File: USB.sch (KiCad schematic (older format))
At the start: 25 parts, among them J1 USB_C_Receptacle, U1 IMX8MM, U2 NX20P3483UK, U6 PTN5110NHQZ

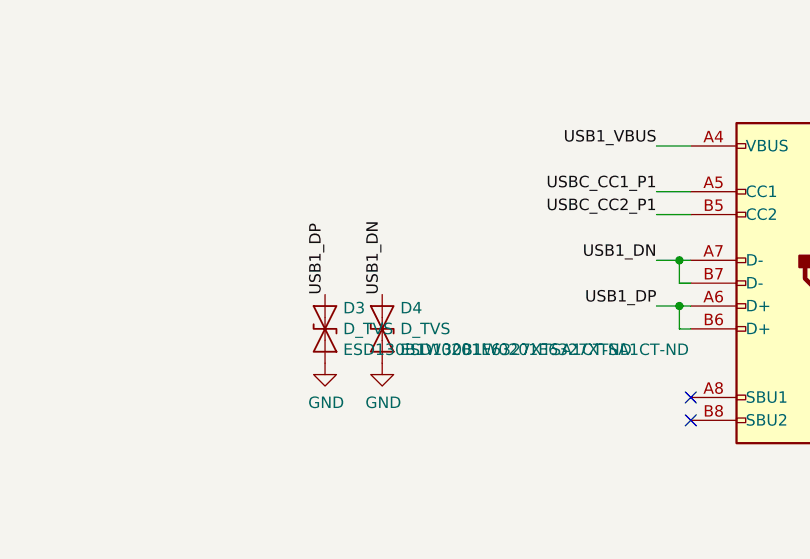
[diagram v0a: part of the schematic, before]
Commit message: Add esd protection to cc lines
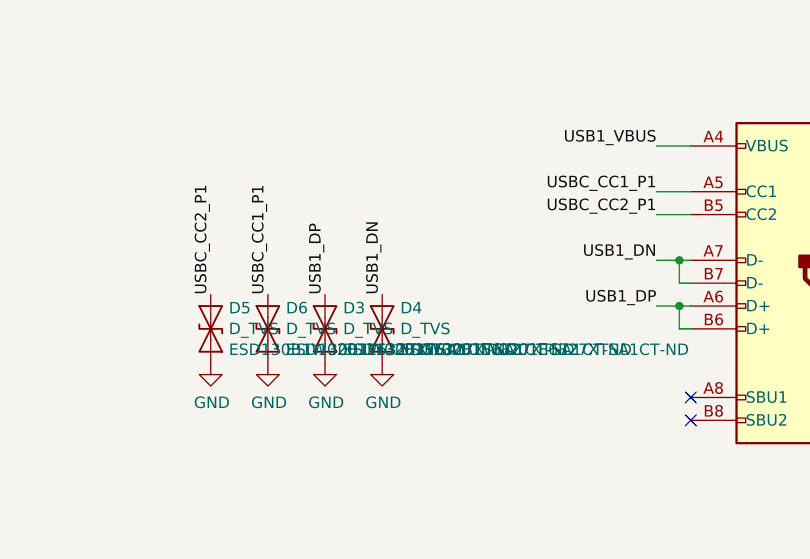
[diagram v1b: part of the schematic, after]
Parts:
- added D5, D6: D_TVS, mxenc:D_TVS_0201_0603Metric, symbol Device:D_TVS
- D3, D4: footprint Diode_SMD:D_0201_0603Metric -> mxenc:D_TVS_0201_0603Metric
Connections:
- net GND: now also D5.2 (A2), D6.2 (A2)
- net USBC_CC1_P1: now also D6.1 (A1)
- net USBC_CC2_P1: now also D5.1 (A1)
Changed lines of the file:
@@
 F 0 "D3" V 12259 7879 50  0000 L CNN
 F 1 "D_TVS" V 12350 7879 50  0000 L CNN
-F 2 "Diode_SMD:D_0201_0603Metric" H 12350 7800 50  0001 C CNN
+F 2 "mxenc:D_TVS_0201_0603Metric" H 12350 7800 50  0001 C CNN
 F 3 "~" H 12350 7800 50  0001 C CNN
 F 4 "ESD130B1W0201E6327XTSA1CT-ND" V 12441 7879 50  0000 L CNN "Vendorpart"
@@
 F 0 "D4" V 12509 7879 50  0000 L CNN
 F 1 "D_TVS" V 12600 7879 50  0000 L CNN
-F 2 "Diode_SMD:D_0201_0603Metric" H 12600 7800 50  0001 C CNN
+F 2 "mxenc:D_TVS_0201_0603Metric" H 12600 7800 50  0001 C CNN
 F 3 "~" H 12600 7800 50  0001 C CNN
 F 4 "ESD130B1W0201E6327XTSA1CT-ND" V 12691 7879 50  0000 L CNN "Vendorpart"
@@
 Text Notes 8300 8250 0    50   ~ 0
 7-bit addr: 0x50
+$Comp
+L Device:D_TVS D6
+U 1 1 5E5F18ED
+P 12100 7800
+F 0 "D6" V 12009 7879 50  0000 L CNN
+F 1 "D_TVS" V 12100 7879 50  0000 L CNN
+F 2 "mxenc:D_TVS_0201_0603Metric" H 12100 7800 50  0001 C CNN
+F 3 "~" H 12100 7800 50  0001 C CNN
+F 4 "ESD130B1W0201E6327XTSA1CT-ND" V 12191 7879 50  0000 L CNN "Vendorpart"
+F 5 "Infineon" H 12100 7800 50  0001 C CNN "Mfgr"
+F 6 "ESD130B1W0201E6327XTSA1" H 12100 7800 50  0001 C CNN "Part"
+	1    12100 7800
+	0    1    1    0
+$EndComp
+$Comp
+L Device:D_TVS D5
+U 1 1 5E5F2B08
+P 11850 7800
+F 0 "D5" V 11759 7879 50  0000 L CNN
+F 1 "D_TVS" V 11850 7879 50  0000 L CNN
+F 2 "mxenc:D_TVS_0201_0603Metric" H 11850 7800 50  0001 C CNN
+F 3 "~" H 11850 7800 50  0001 C CNN
+F 4 "ESD130B1W0201E6327XTSA1CT-ND" V 11941 7879 50  0000 L CNN "Vendorpart"
+F 5 "Infineon" H 11850 7800 50  0001 C CNN "Mfgr"
+F 6 "ESD130B1W0201E6327XTSA1" H 11850 7800 50  0001 C CNN "Part"
+	1    11850 7800
+	0    1    1    0
+$EndComp
+Text Label 12100 7650 1    50   ~ 0
+USBC_CC1_P1
+Text Label 11850 7650 1    50   ~ 0
+USBC_CC2_P1
+$Comp
+L power:GND #PWR0254
+U 1 1 5E5F61FF
+P 11850 7950
+F 0 "#PWR0254" H 11850 7700 50  0001 C CNN
+F 1 "GND" H 11855 7777 50  0000 C CNN
+F 2 "" H 11850 7950 50  0001 C CNN
+F 3 "" H 11850 7950 50  0001 C CNN
+	1    11850 7950
+	1    0    0    -1
+$EndComp
+$Comp
+L power:GND #PWR0255
+U 1 1 5E5F668A
+P 12100 7950
+F 0 "#PWR0255" H 12100 7700 50  0001 C CNN
+F 1 "GND" H 12105 7777 50  0000 C CNN
+F 2 "" H 12100 7950 50  0001 C CNN
+F 3 "" H 12100 7950 50  0001 C CNN
+	1    12100 7950
+	1    0    0    -1
+$EndComp
 $EndSCHEMATC

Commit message: Fix up main power supply decoupling
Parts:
- C93: footprint Capacitor_SMD:C_1210_3225Metric -> Capacitor_SMD:C_1206_3216Metric; Mfgr Murata -> TDK; Part GRM32EC81C476ME15L -> C3216X5R1E476M160AC; Vendorpart 490-9968-1-ND -> 445-8047-1-ND
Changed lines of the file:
@@
 F 0 "C93" H 11815 2096 50  0000 L CNN
 F 1 "47uF" H 11815 2005 50  0000 L CNN
-F 2 "Capacitor_SMD:C_1210_3225Metric" H 11738 1900 50  0001 C CNN
+F 2 "Capacitor_SMD:C_1206_3216Metric" H 11738 1900 50  0001 C CNN
 F 3 "~" H 11700 2050 50  0001 C CNN
-F 4 "Murata" H 11700 2050 50  0001 C CNN "Mfgr"
-F 5 "GRM32EC81C476ME15L" H 11700 2050 50  0001 C CNN "Part"
-F 6 "490-9968-1-ND" H 11700 2050 50  0001 C CNN "Vendorpart"
+F 4 "TDK" H 11700 2050 50  0001 C CNN "Mfgr"
+F 5 "C3216X5R1E476M160AC" H 11700 2050 50  0001 C CNN "Part"
+F 6 "445-8047-1-ND" H 11700 2050 50  0001 C CNN "Vendorpart"
 	1    11700 2050
 	1    0    0    -1

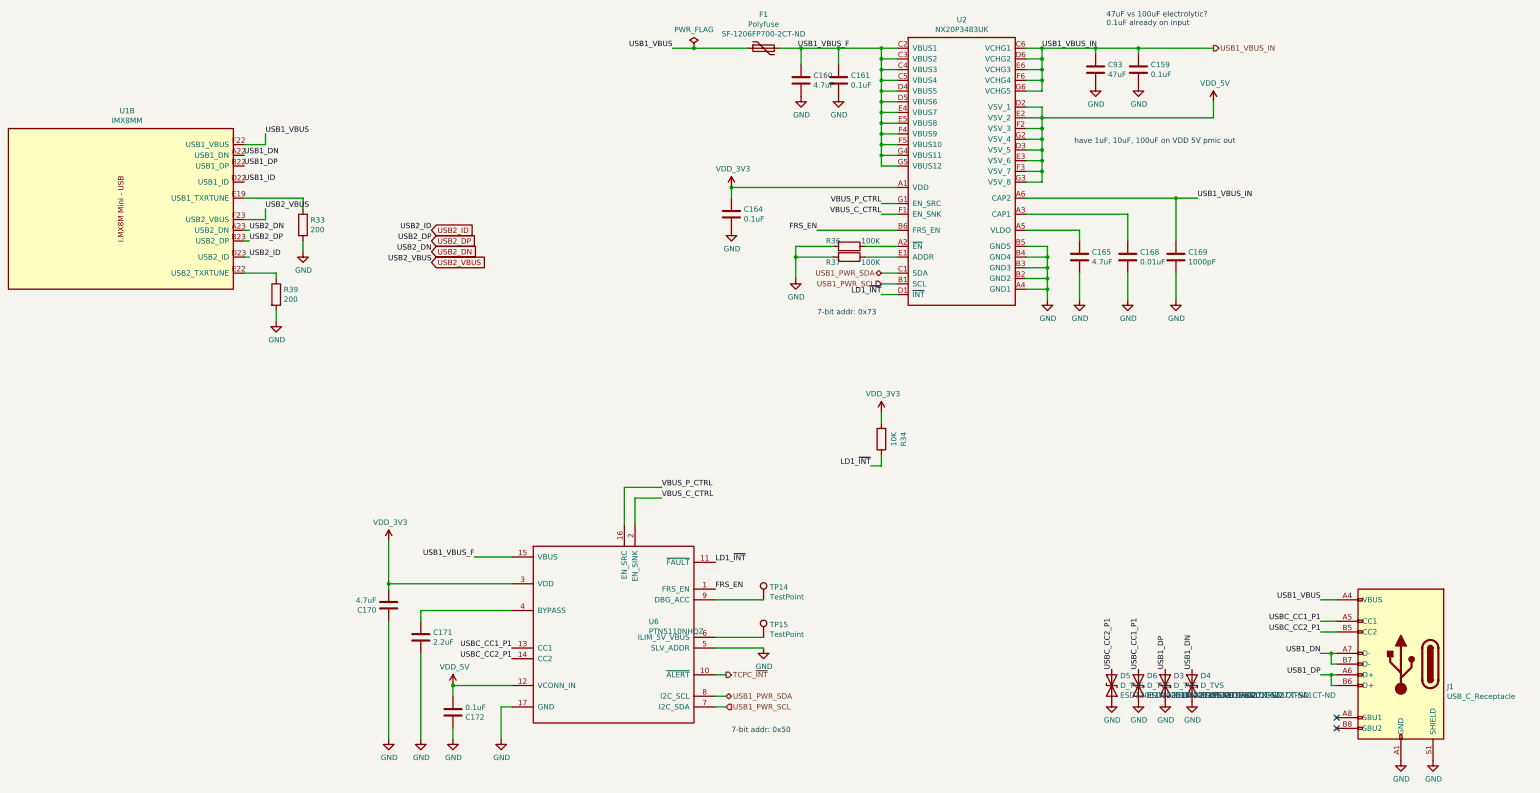
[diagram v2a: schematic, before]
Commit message: Change power input to JST-PH
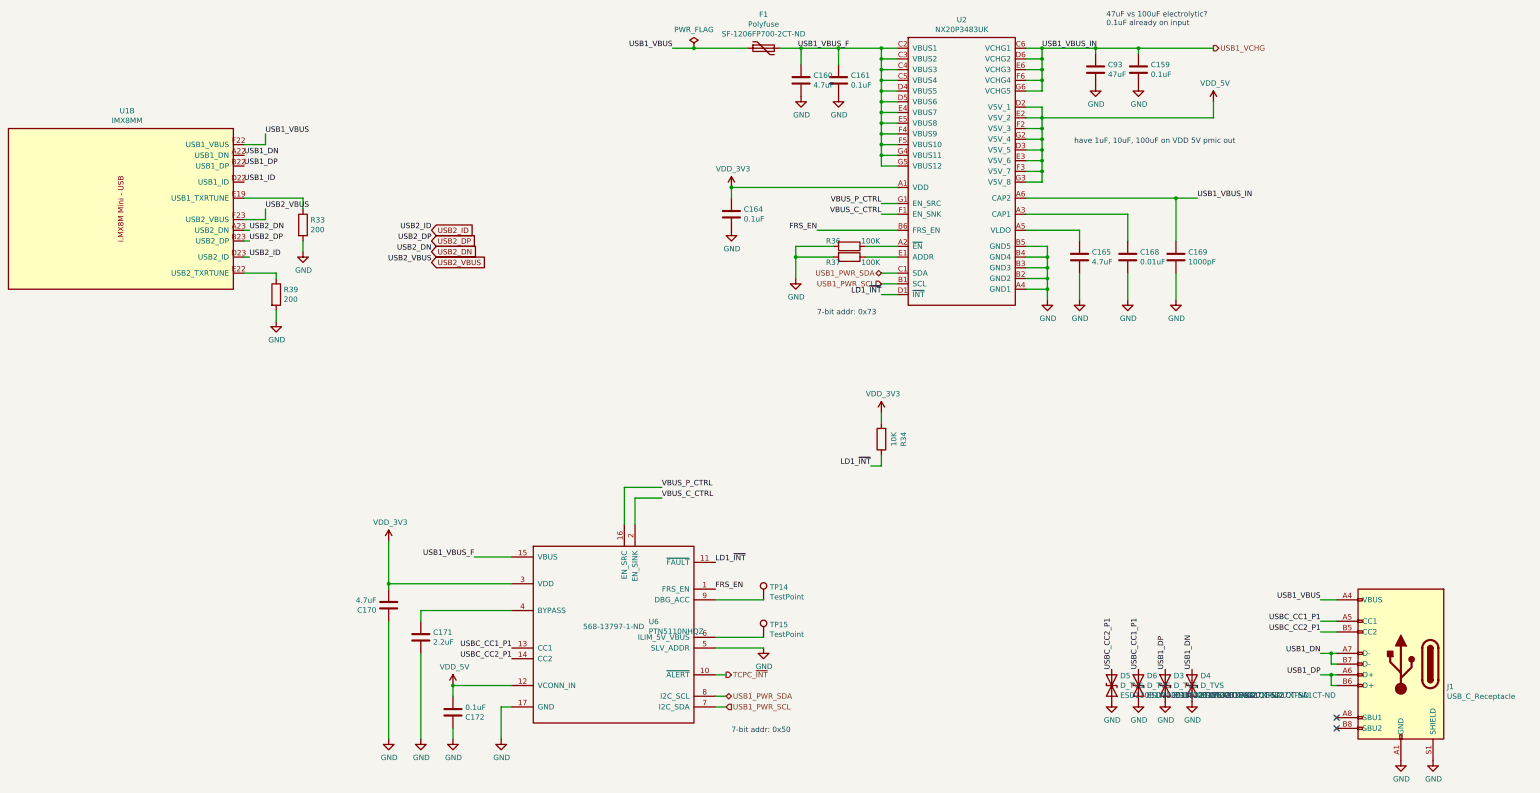
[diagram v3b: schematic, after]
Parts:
- U6: Mfgr (none) -> NXP; Part (none) -> PTN5110NHQZ; Vendorpart (none) -> 568-13797-1-ND
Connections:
- net USB1_VBUS_IN renamed USB1_VCHG
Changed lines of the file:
@@
 	12650 3250 12450 3250
 Connection ~ 12450 3250
-$Comp
-L Device:C C159
-U 1 1 5E2A53AF
-P 12100 2050
-F 0 "C159" H 12215 2096 50  0000 L CNN
-F 1 "0.1uF" H 12215 2005 50  0000 L CNN
-F 2 "Capacitor_SMD:C_0402_1005Metric" H 12138 1900 50  0001 C CNN
-F 3 "~" H 12100 2050 50  0001 C CNN
-F 4 "Murata" H 12100 2050 50  0001 C CNN "Mfgr"
-F 5 "GRM155R71E104KE14J" H 12100 2050 50  0001 C CNN "Part"
-F 6 "490-14603-1-ND" H 12100 2050 50  0001 C CNN "Vendorpart"
-	1    12100 2050
-	1    0    0    -1
-$EndComp
-$Comp
-L Device:C C93
-U 1 1 5E2A61B9
-P 11700 2050
-F 0 "C93" H 11815 2096 50  0000 L CNN
-F 1 "47uF" H 11815 2005 50  0000 L CNN
-F 2 "Capacitor_SMD:C_1206_3216Metric" H 11738 1900 50  0001 C CNN
-F 3 "~" H 11700 2050 50  0001 C CNN
-F 4 "TDK" H 11700 2050 50  0001 C CNN "Mfgr"
-F 5 "C3216X5R1E476M160AC" H 11700 2050 50  0001 C CNN "Part"
-F 6 "445-8047-1-ND" H 11700 2050 50  0001 C CNN "Vendorpart"
-	1    11700 2050
-	1    0    0    -1
-$EndComp
-Wire Wire Line
-	11700 1900 11700 1850
-Connection ~ 11700 1850
-Wire Wire Line
-	11700 1850 11200 1850
-Wire Wire Line
-	12100 1850 12100 1900
-Wire Wire Line
-	11700 1850 12100 1850
-$Comp
-L power:GND #PWR0206
-U 1 1 5E2BF50F
-P 11700 2200
-F 0 "#PWR0206" H 11700 1950 50  0001 C CNN
-F 1 "GND" H 11705 2027 50  0000 C CNN
-F 2 "" H 11700 2200 50  0001 C CNN
-F 3 "" H 11700 2200 50  0001 C CNN
-	1    11700 2200
-	1    0    0    -1
-$EndComp
-$Comp
-L power:GND #PWR0207
-U 1 1 5E2BFA4F
-P 12100 2200
-F 0 "#PWR0207" H 12100 1950 50  0001 C CNN
-F 1 "GND" H 12105 2027 50  0000 C CNN
-F 2 "" H 12100 2200 50  0001 C CNN
-F 3 "" H 12100 2200 50  0001 C CNN
-	1    12100 2200
-	1    0    0    -1
-$EndComp
 Text HLabel 12800 1850 2    50   Output ~ 0
-USB1_VBUS_IN
-Wire Wire Line
-	12800 1850 12100 1850
-Connection ~ 12100 1850
+USB1_VCHG
 Wire Wire Line
 	11050 2400 11200 2400
@@
 F 2 "mxenc:HX2QFN-16_EP_2.85x2.85_Pitch0.4mm" H 7200 7250 50  0001 C CNN
 F 3 "" H 7200 7250 50  0001 C CNN
+F 4 "568-13797-1-ND" H 7200 7250 50  0000 C CNN "Vendorpart"
+F 5 "NXP" H 7200 7250 50  0001 C CNN "Mfgr"
+F 6 "PTN5110NHQZ" H 7200 7250 50  0001 C CNN "Part"
 	1    7200 7250
 	1    0    0    -1
@@
 	1    0    0    -1
 $EndComp
+$Comp
+L power:GND #PWR0207
+U 1 1 5E2BFA4F
+P 12100 2200
+F 0 "#PWR0207" H 12100 1950 50  0001 C CNN
+F 1 "GND" H 12105 2027 50  0000 C CNN
+F 2 "" H 12100 2200 50  0001 C CNN
+F 3 "" H 12100 2200 50  0001 C CNN
+	1    12100 2200
+	1    0    0    -1
+$EndComp
+$Comp
+L power:GND #PWR0206
+U 1 1 5E2BF50F
+P 11700 2200
+F 0 "#PWR0206" H 11700 1950 50  0001 C CNN
+F 1 "GND" H 11705 2027 50  0000 C CNN
+F 2 "" H 11700 2200 50  0001 C CNN
+F 3 "" H 11700 2200 50  0001 C CNN
+	1    11700 2200
+	1    0    0    -1
+$EndComp
+Wire Wire Line
+	12800 1850 12100 1850
+Connection ~ 12100 1850
+Wire Wire Line
+	12100 1850 12100 1900
+Wire Wire Line
+	11700 1850 12100 1850
+Wire Wire Line
+	11700 1850 11200 1850
+Connection ~ 11700 1850
+Wire Wire Line
+	11700 1900 11700 1850
+$Comp
+L Device:C C93
+U 1 1 5E2A61B9
+P 11700 2050
+F 0 "C93" H 11815 2096 50  0000 L CNN
+F 1 "47uF" H 11815 2005 50  0000 L CNN
+F 2 "Capacitor_SMD:C_1206_3216Metric" H 11738 1900 50  0001 C CNN
+F 3 "~" H 11700 2050 50  0001 C CNN
+F 4 "TDK" H 11700 2050 50  0001 C CNN "Mfgr"
+F 5 "C3216X5R1E476M160AC" H 11700 2050 50  0001 C CNN "Part"
+F 6 "445-8047-1-ND" H 11700 2050 50  0001 C CNN "Vendorpart"
+	1    11700 2050
+	1    0    0    -1
+$EndComp
+$Comp
+L Device:C C159
+U 1 1 5E2A53AF
+P 12100 2050
+F 0 "C159" H 12215 2096 50  0000 L CNN
+F 1 "0.1uF" H 12215 2005 50  0000 L CNN
+F 2 "Capacitor_SMD:C_0402_1005Metric" H 12138 1900 50  0001 C CNN
+F 3 "~" H 12100 2050 50  0001 C CNN
+F 4 "Murata" H 12100 2050 50  0001 C CNN "Mfgr"
+F 5 "GRM155R71E104KE14J" H 12100 2050 50  0001 C CNN "Part"
+F 6 "490-14603-1-ND" H 12100 2050 50  0001 C CNN "Vendorpart"
+	1    12100 2050
+	1    0    0    -1
+$EndComp

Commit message: Switch 5V buck for 1S battery charger boost
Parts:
- C160: footprint Capacitor_SMD:C_1210_3225Metric -> Capacitor_SMD:C_0603_1608Metric; Mfgr Yageo -> Taiyo Yuden; Part CC1210MKX7R6BB475 -> JMK107C6475MA-T; Vendorpart 311-3539-1-ND -> 587-4905-1-ND
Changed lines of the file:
@@
 	7750 1850 7950 1850
-$Comp
-L Device:C C160
-U 1 1 5E14CE67
-P 8950 2150
-F 0 "C160" H 9065 2196 50  0000 L CNN
-F 1 "4.7uF" H 9065 2105 50  0000 L CNN
-F 2 "Capacitor_SMD:C_1210_3225Metric" H 8988 2000 50  0001 C CNN
-F 3 "~" H 8950 2150 50  0001 C CNN
-F 4 "Yageo" H 8950 2150 50  0001 C CNN "Mfgr"
-F 5 "CC1210MKX7R6BB475" H 8950 2150 50  0001 C CNN "Part"
-F 6 "311-3539-1-ND" H 8950 2150 50  0001 C CNN "Vendorpart"
-	1    8950 2150
-	1    0    0    -1
-$EndComp
 $Comp
 L Device:C C161
@@
 	1    0    0    -1
 $EndComp
-Text Notes 11800 1650 0    50   ~ 0
-47uF vs 100uF electrolytic?\n0.1uF already on input
 Text Notes 11500 2750 0    50   ~ 0
 have 1uF, 10uF, 100uF on VDD 5V pmic out
@@
 	1    0    0    -1
 $EndComp
+Text Notes 11800 1650 0    50   ~ 0
+47uF vs 100uF electrolytic?\n0.1uF already on input
+$Comp
+L Device:C C160
+U 1 1 5F1F8DAE
+P 8950 2150
+F 0 "C160" H 9065 2196 50  0000 L CNN
+F 1 "4.7uF" H 9065 2105 50  0000 L CNN
+F 2 "Capacitor_SMD:C_0603_1608Metric" H 8988 2000 50  0001 C CNN
+F 3 "~" H 8950 2150 50  0001 C CNN
+F 4 "Taiyo Yuden" H 8950 2150 50  0001 C CNN "Mfgr"
+F 5 "JMK107C6475MA-T" H 8950 2150 50  0001 C CNN "Part"
+F 6 "587-4905-1-ND" H 8950 2150 50  0001 C CNN "Vendorpart"
+	1    8950 2150
+	1    0    0    -1
+$EndComp

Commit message: Set up for battery NTC and add a power button
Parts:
- J1: symbol Connector:USB_C_Receptacle_USB2.0 -> mxenc:USB_C_Receptacle_USB2.0
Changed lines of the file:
@@
 EESchema Schematic File Version 4
-LIBS:mxenc-cache
-EELAYER 29 0
+EELAYER 30 0
 EELAYER END
 $Descr USLedger 17000 11000
 encoding utf-8
 Sheet 10 10
-Title ""
-Date ""
-Rev ""
-Comp ""
+Title "kimχ micro"
+Date "2020-03-05"
+Rev "0.9"
+Comp "GroupGets"
 Comment1 ""
 Comment2 ""
@@
 $EndComp
 $Comp
-L Connector:USB_C_Receptacle_USB2.0 J1
+L mxenc:USB_C_Receptacle_USB2.0 J1
 U 1 1 5D6908E4
 P 14550 7600
